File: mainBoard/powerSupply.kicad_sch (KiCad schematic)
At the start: 24 parts, among them J1 1366005, J2 Conn_01x02, J3 Conn_01x02, SW1 SW_SPST, U1 MCP1727T-3302E/SN

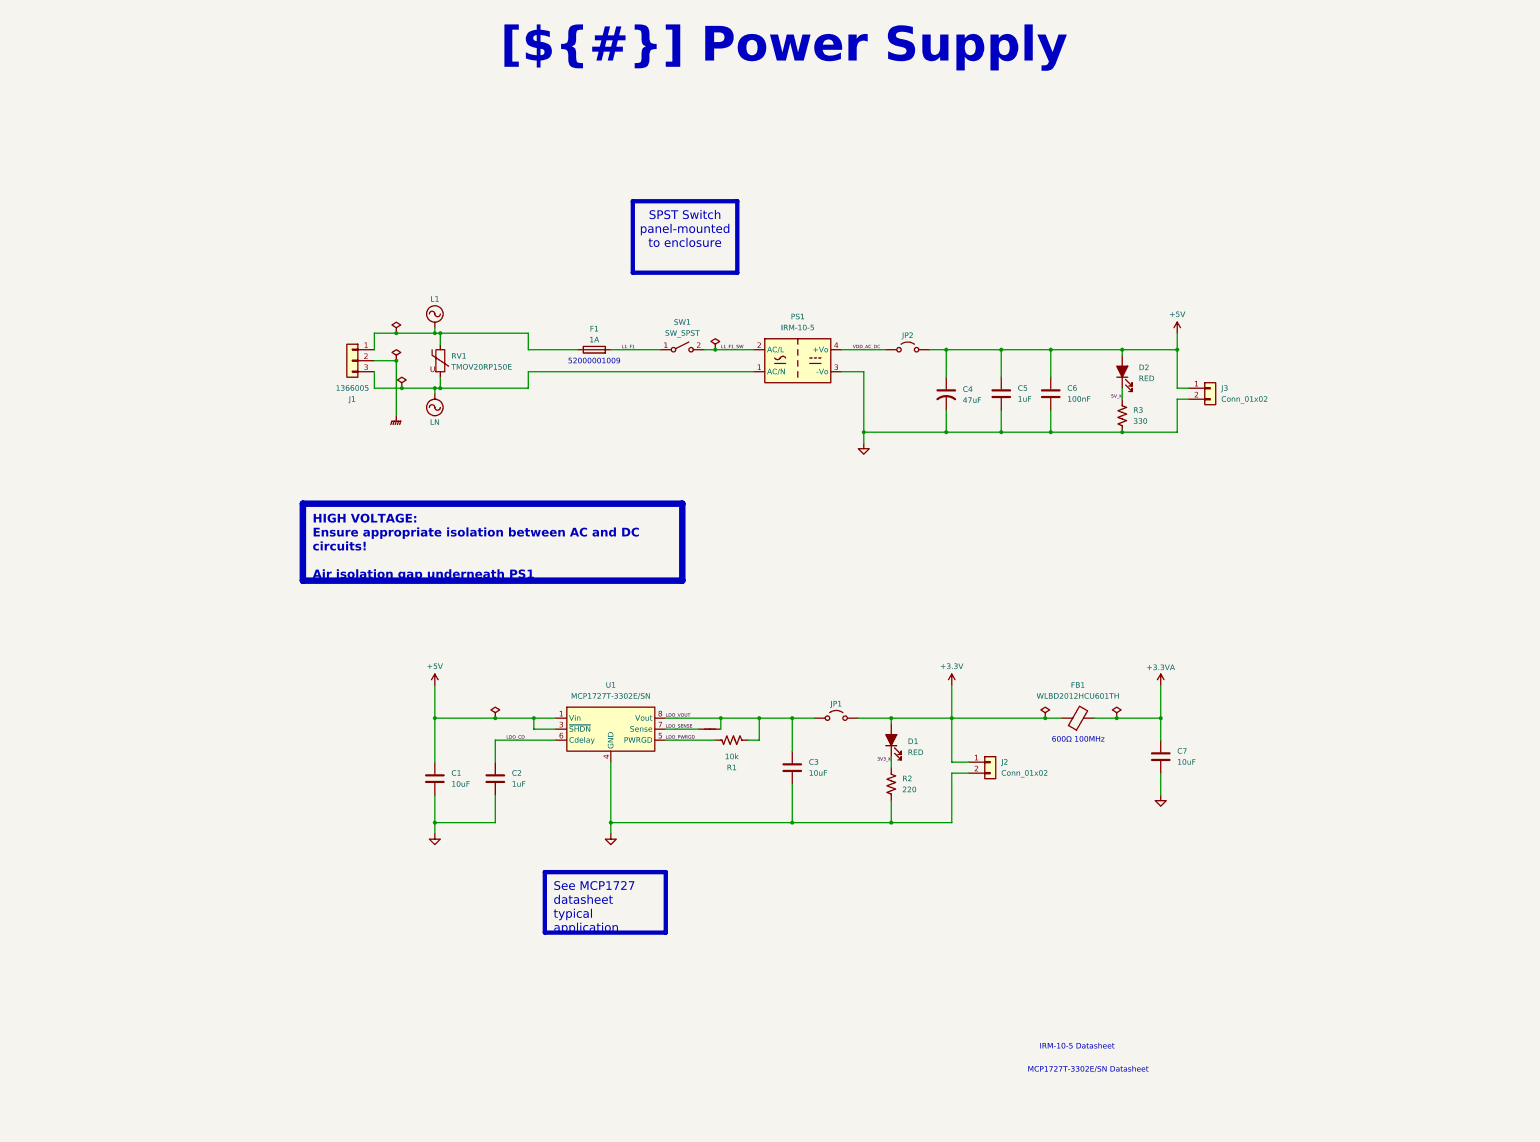
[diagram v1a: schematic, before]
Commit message: tweak schematic for changes from 6-17-2026
major structural changes, see daily note from obsidian
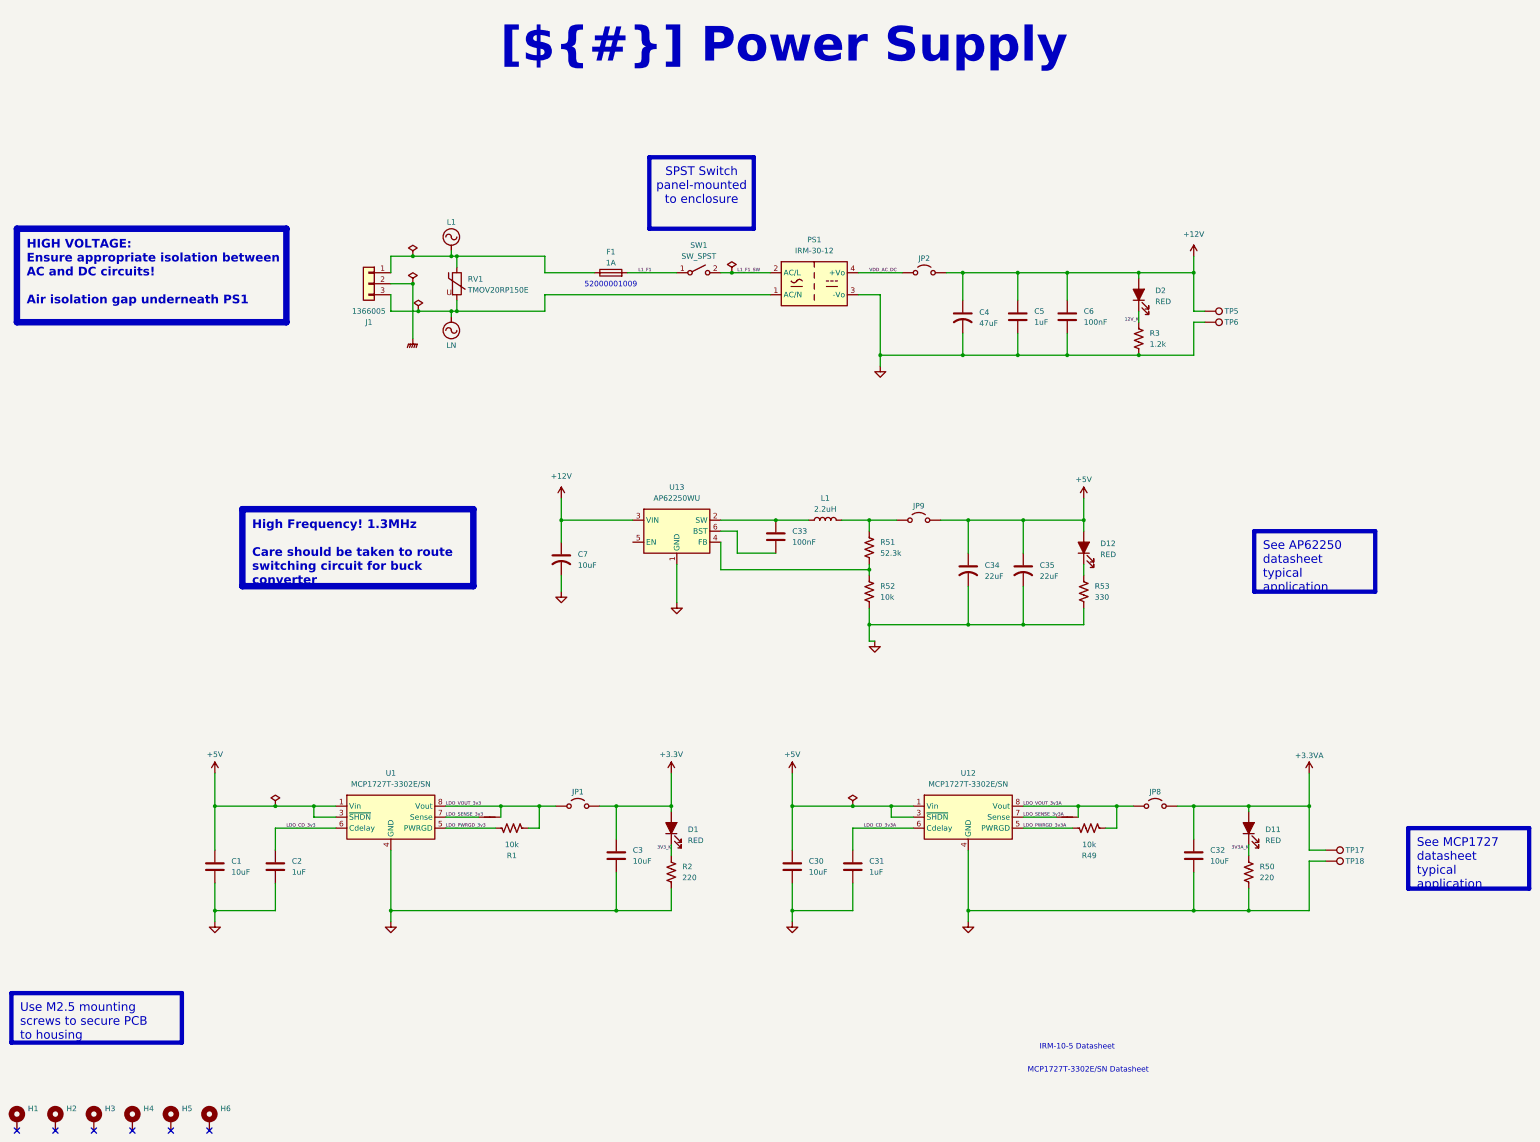
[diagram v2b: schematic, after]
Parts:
- removed C7: 10uF, Capacitor_SMD:C_0805_2012Metric_Pad1.18x1.45mm_HandSolder, symbol Device:C
- removed FB1: WLBD2012HCU601TH, Inductor_SMD:L_0805_2012Metric_Pad1.05x1.20mm_HandSolder, symbol Device:FerriteBead
- removed J2, J3: Conn_01x02, TerminalBlock_Phoenix:TerminalBlock_Phoenix_MKDS-1,5-2-5.08_1x02_P5.08mm_Horizontal, symbol Connector_Generic:Conn_01x02
- added C30, C32: 10uF, Capacitor_SMD:C_0805_2012Metric_Pad1.18x1.45mm_HandSolder, symbol Device:C
- added C31: 1uF, Capacitor_SMD:C_0805_2012Metric_Pad1.18x1.45mm_HandSolder, symbol Device:C
- added C33: 100nF, Capacitor_SMD:C_0603_1608Metric_Pad1.08x0.95mm_HandSolder, symbol Device:C
- added C34, C35: 22uF, Capacitor_THT:C_Radial_D5.0mm_H11.0mm_P2.00mm, symbol Device:C_US
- added C7: 10uF, Capacitor_THT:C_Radial_D5.0mm_H11.0mm_P2.00mm, symbol Device:C_US
- added D11, D12: RED, LED_SMD:LED_0603_1608Metric_Pad1.05x0.95mm_HandSolder, symbol Device:LED_Filled
- added H1, H2, H3, H4, H5, H6: MountingHole_Pad, MountingHole:MountingHole_2.7mm, symbol Mechanical:MountingHole_Pad
- added JP8, JP9: Jumper_2_Open, Connector_PinHeader_2.54mm:PinHeader_1x02_P2.54mm_Vertical, symbol Jumper:Jumper_2_Open
- added L1: 2.2uH, symbol Device:L
- added NT2: NetTie_2, NetTie:NetTie-2_SMD_Pad0.5mm, symbol Device:NetTie_2
- added R49, R52: 10k, Resistor_SMD:R_0603_1608Metric_Pad0.98x0.95mm_HandSolder, symbol Device:R_US
- added R50: 220, Resistor_SMD:R_0603_1608Metric_Pad0.98x0.95mm_HandSolder, symbol Device:R_US
- added R51: 52.3k, Resistor_SMD:R_0603_1608Metric_Pad0.98x0.95mm_HandSolder, symbol Device:R_US
- added R53: 330, Resistor_SMD:R_0603_1608Metric_Pad0.98x0.95mm_HandSolder, symbol Device:R_US
- added TP17, TP18, TP5, TP6: TestPoint, TestPoint:TestPoint_Pad_4.0x4.0mm, symbol Connector:TestPoint
- added U12: MCP1727T-3302E/SN, Package_SO:SOIC-8_3.9x4.9mm_P1.27mm, symbol Regulator_Linear:MCP1727-3302xSN
- added U13: AP62250WU, Package_TO_SOT_SMD:TSOT-23-6_HandSoldering, symbol Regulator_Switching:AP62250WU
- C4: footprint Capacitor_THT:C_Radial_D5.0mm_H5.0mm_P2.00mm -> Capacitor_THT:C_Radial_D5.0mm_H11.0mm_P2.00mm
- PS1: value IRM-10-5 -> IRM-30-12; footprint Converter_ACDC:Converter_ACDC_MeanWell_IRM-10-xx_THT -> IRM-30:IRM-30_MWU
- R3: value 330 -> 1.2k
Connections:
- net +3.3V: now also C3.1
- net +3.3VA: now also C32.1, D11.2 (A), JP8.2 (B), TP17.1
- net +5V: now also C30.1, C34.1, C35.1, D12.2 (A), JP9.2 (B), U12.1 (Vin), U12.2 (Vin), U12.3 (~{SHDN}); no longer C4.1, C5.1, C6.1, D2.2 (A), JP2.2 (B)
- net GND: now also C30.2, C31.2, C32.2, C34.2, C35.2, C7.2, R50.2, R52.2, R53.2, TP18.1, TP6.1, U12.4 (GND), U13.1 (GND)
- net 5V_K renamed 12V_K
- net LDO_CD renamed LDO_CD_3v3
- net LDO_PWRGD renamed LDO_PWRGD_3v3
- net LDO_SENSE renamed LDO_SENSE_3v3
- net LDO_VOUT renamed LDO_VOUT_3v3
- net LDO_VOUT_3v3: no longer C3.1
- new net: D12.1 (K), R53.1
- new net: JP9.1 (A), L1.2, R51.1
- new net: C33.1, L1.1, U13.2 (SW)
- new net: R51.2, R52.1, U13.4 (FB)
- new net: C33.2, U13.6 (BST)
- new net +12V: C4.1, C5.1, C6.1, C7.1, D2.2 (A), JP2.2 (B), TP5.1, U13.3 (VIN)
- new net 3V3A_K: D11.1 (K), R50.1
- new net LDO_CD_3v3A: C31.1, U12.6 (Cdelay)
- new net LDO_PWRGD_3v3A: R49.2, U12.5 (PWRGD)
- new net LDO_SENSE_3v3A: NT2.1, U12.7 (Sense)
- new net LDO_VOUT_3v3A: JP8.1 (A), NT2.2, R49.1, U12.8 (Vout)
- no-connect marks 0 -> 6
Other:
- note removed: "600Ω 100MHz"
- moved on the sheet: C1, C2, C3, C4, C5, C6, D1, D2, F1, J1, JP1, JP2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

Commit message: work on pcb design
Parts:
- L1: footprint (none) -> Inductor_SMD:L_1008_2520Metric_Pad1.43x2.20mm_HandSolder; Part Number (none) -> LQM2HPN2R2MG0L
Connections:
- no-connect marks 6 -> 7
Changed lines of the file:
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@@
 		(at 68.58 271.78)
 	)
+	(no_connect
+		(at 175.26 135.89)
+	)
 	(wire
 		(pts
@@
 		(on_board yes)
 		(dnp no)
-		(fields_autoplaced yes)
 		(property "Reference" "L1"
 			(at 219.71 125.73 90)
@@
 			)
 		)
-		(property "Footprint" ""
+		(property "Footprint" "Inductor_SMD:L_1008_2520Metric_Pad1.43x2.20mm_HandSolder"
 			(at 219.71 130.81 0)
 			(effects
@@
 			)
 		)
+		(property "Part Number" "LQM2HPN2R2MG0L"
+			(at 219.71 123.19 90)
+			(effects
+				(font
+					(size 1.27 1.27)
+				)
+			)
+		)

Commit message: working on pcb layout after bringing in work from laptop
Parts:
- C10: renamed from C35; footprint Capacitor_THT:C_Radial_D5.0mm_H11.0mm_P2.00mm -> Capacitor_SMD:C_1206_3216Metric_Pad1.33x1.80mm_HandSolder; symbol Device:C_US -> Device:C; part number (none) -> CL31A226MOCLNNC
- C11: renamed from C5; part number (none) -> CL21B105KAFNNNE
- C13: renamed from C32; part number (none) -> CL21A106KQFNNNE
- C3: renamed from C7; footprint Capacitor_THT:C_Radial_D5.0mm_H11.0mm_P2.00mm -> KemetA765:CAPAE830X730N; symbol Device:C_US -> Device:C_Polarized; part number (none) -> A765KG106M1ELAE035
- C8: renamed from C34; footprint Capacitor_THT:C_Radial_D5.0mm_H11.0mm_P2.00mm -> Capacitor_SMD:C_1206_3216Metric_Pad1.33x1.80mm_HandSolder; symbol Device:C_US -> Device:C; part number (none) -> CL31A226MOCLNNC
- C9: renamed from C4; footprint Capacitor_THT:C_Radial_D5.0mm_H11.0mm_P2.00mm -> Capacitor_SMD:C_Elec_6.3x5.8; symbol Device:C_US -> Device:C_Polarized; part number (none) -> A768EB476M1VLAE042
- L1: Part Number LQM2HPN2R2MG0L -> (none); part number (none) -> MAMK2520T2R2M
- renumbered C6 to C12, C3 to C4, C33 to C5, C30 to C6, C31 to C7, D12 to D2, D2 to D3, D11 to D4, JP9 to JP2, JP2 to JP3, JP8 to JP4, R51 to R3, R52 to R4, R49 to R5, R53 to R6, R3 to R7, R50 to R8, TP5 to TP1, TP6 to TP2, TP17 to TP3, TP18 to TP4, U13 to U2, U12 to U3
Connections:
- net +5V: no longer C10.1, C8.1
- net 5V_K: now reaches D2.1 (K), R6.1
- net 5V_BUCK_VOUT: now reaches JP2.1 (A), L1.2, R3.1
- net 5V_BUCK_VOUT: now also C10.1, C8.1
- net 5V_BUCK_SW: now reaches C5.1, L1.1, U2.2 (SW)
- net 5V_BUCK_FB: now reaches R3.2, R4.1, U2.4 (FB)
- net 5V_BUCK_BST: now reaches C5.2, U2.6 (BST)
- net VDD_AC_DC renamed AC_DC_+12V
- no-connect marks 7 -> 6
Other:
- note added: "A765KG106M1ELAE035"
- note added: "A768EB476M1VLAE042"
- note added: "CL21A106KQFNNNE"
- note added: "CL21B105KAFNNNE"
- note added: "CL31A226MOCLNNC x2"
- note added: "MAMK2520T2R2M"
- moved on the sheet: C10, C11, C12, C5, C8, D2, D3, F1, J1, JP2, JP3, L1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

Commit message: board routing nearly complete
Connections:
- no-connect marks 6 -> 7
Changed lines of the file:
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@@
+	)
+	(no_connect
+		(at 172.72 142.24)
 	)
 	(no_connect

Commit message: board tweaked, sent for review
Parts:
- C2, C7: value 1uF -> 100nF
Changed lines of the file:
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@@
 			)
 		)
-		(property "Value" "1uF"
+		(property "Value" "100nF"
 			(at 229.87 212.0899 0)
 			(show_name no)
@@
 			)
 		)
-		(property "Description" "5V, 2A, 10W, Isolated, AC-DC, 222A(IRM10)"
+		(property "Description" "30W, 12VDC out, 120VAC in, encapsulated power suppy module"
 			(at 228.6 83.82 0)
 			(hide yes)
@@
 			)
 		)
-		(property "Value" "1uF"
+		(property "Value" "100nF"
 			(at 96.52 212.0899 0)
 			(show_name no)

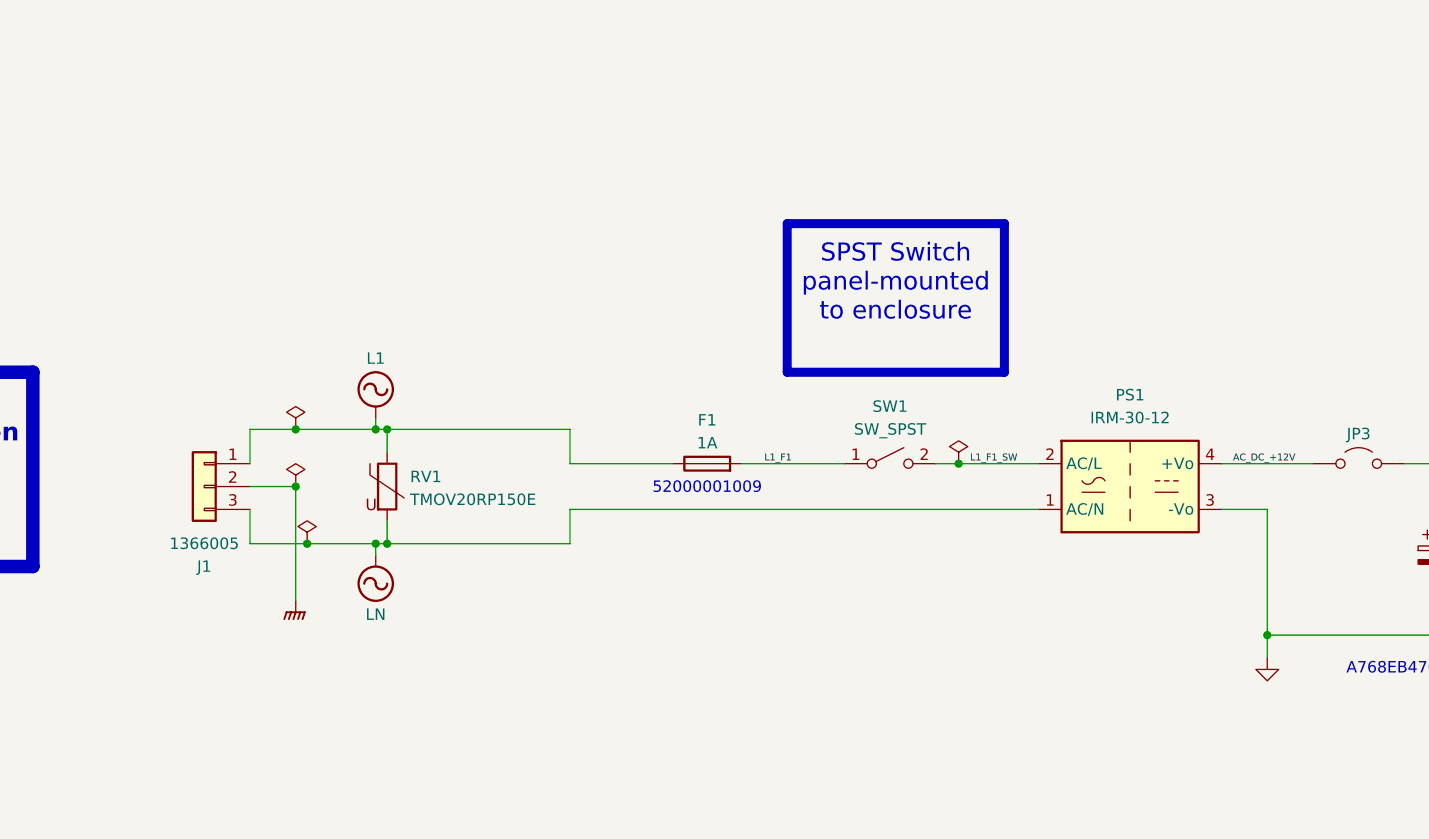
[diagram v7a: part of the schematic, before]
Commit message: reworked AC switching and fusing
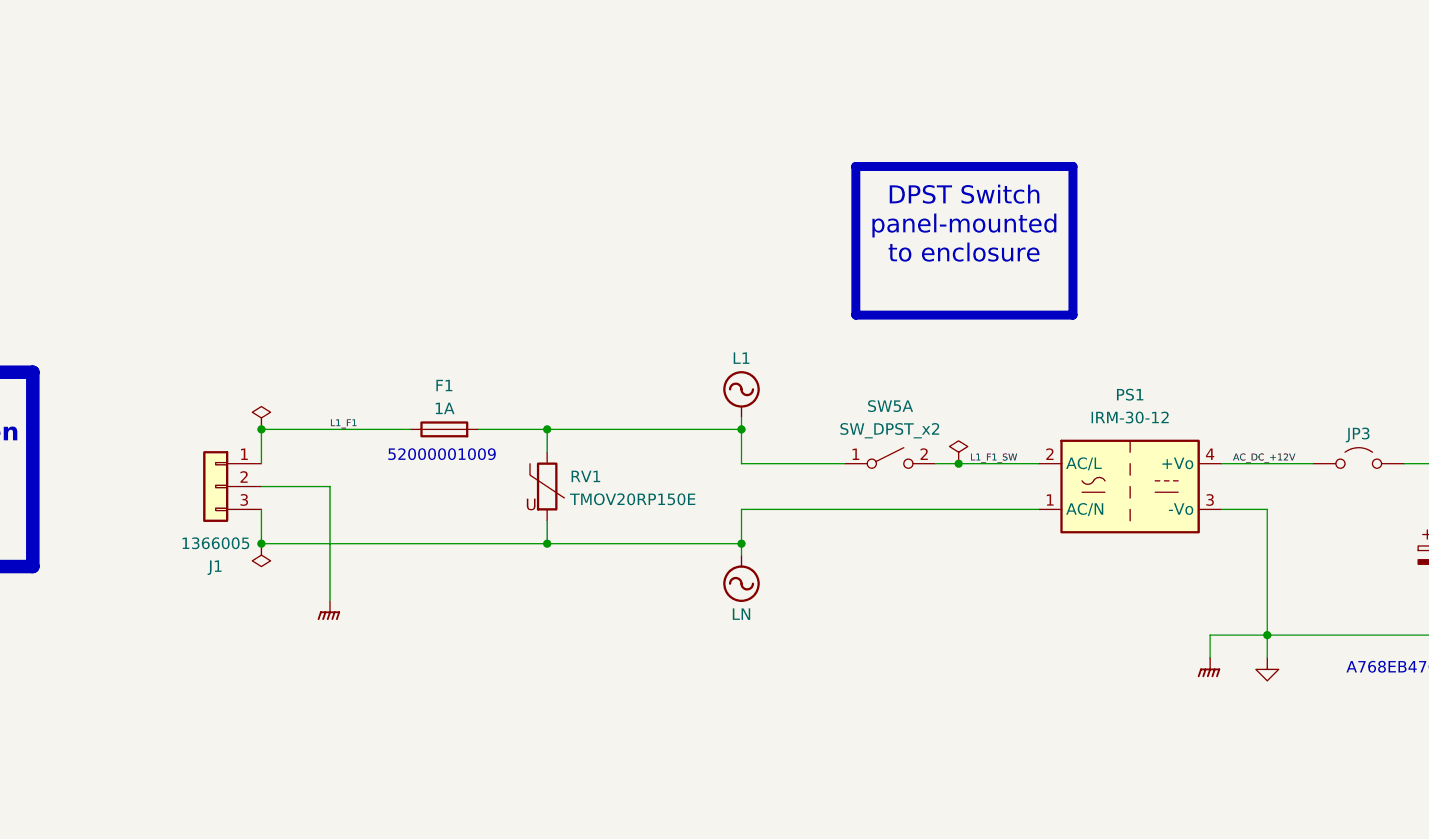
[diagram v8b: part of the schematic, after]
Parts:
- removed SW1: SW_SPST, TerminalBlock_Phoenix:TerminalBlock_Phoenix_MKDS-1,5-2-5.08_1x02_P5.08mm_Horizontal, symbol Switch:SW_SPST
- added SW5: SW_DPST_x2, TerminalBlock_Phoenix:TerminalBlock_Phoenix_MKDS-1,5-2-5.08_1x02_P5.08mm_Horizontal, symbol Switch:SW_DPST_x2
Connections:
- net GNDPWR is gone; now on net GND: J1.2 (Pin_2)
- net L1: now also F1.2, SW5.1 (A); no longer F1.1, J1.1 (Pin_1)
- net L1_F1: now also F1.1, J1.1 (Pin_1); no longer F1.2
- net L1_F1_SW: now also SW5.2 (B)
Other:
- moved on the sheet: F1, J1, RV1
